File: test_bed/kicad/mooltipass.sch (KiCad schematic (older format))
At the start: 14 parts, among them CON1 AVR-ISP-6, P1 CONN_8, P2 CONN_6, P3 CONN_10, P4 CONN_8, P5 CONN_1, P6 CONN_1, P7 CONN_1, P8 CONN_1

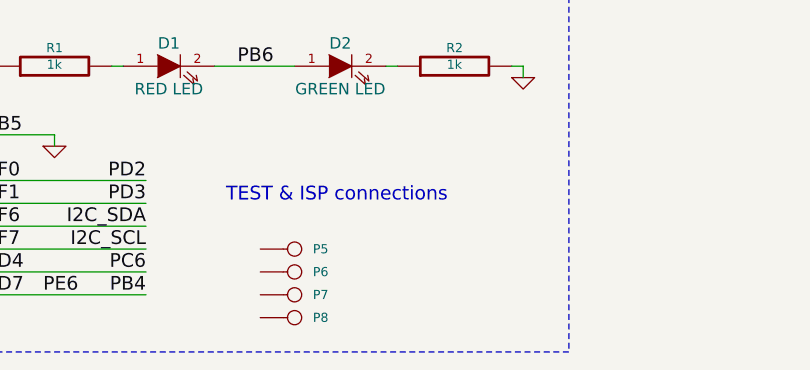
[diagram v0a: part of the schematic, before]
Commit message: mooltipass electrical test bed complete
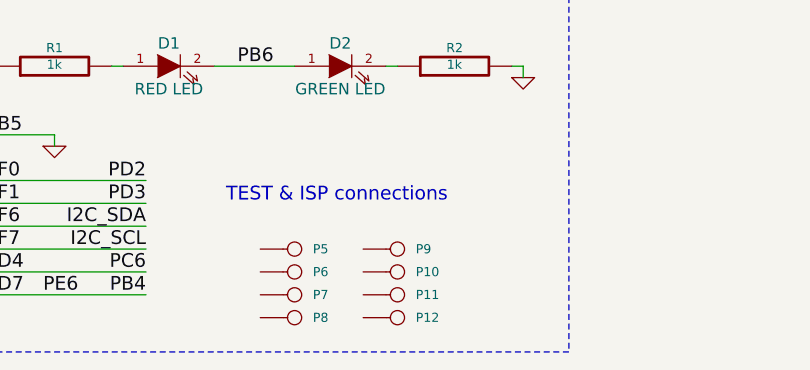
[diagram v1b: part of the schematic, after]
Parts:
- added P10, P11, P12, P9: CONN_1, symbol CONN_1
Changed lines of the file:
@@
 A5
 $Comp
-L +5V #PWR01
+L +5V #PWR3
 U 1 1 53011242
 P 2150 3600
-F 0 "#PWR01" H 2150 3690 20  0001 C CNN
+F 0 "#PWR3" H 2150 3690 20  0001 C CNN
 F 1 "+5V" H 2150 3690 30  0000 C CNN
 F 2 "" H 2150 3600 60  0000 C CNN
@@
 $EndComp
 $Comp
-L GND #PWR02
+L GND #PWR2
 U 1 1 5301124C
 P 2000 4400
-F 0 "#PWR02" H 2000 4400 30  0001 C CNN
+F 0 "#PWR2" H 2000 4400 30  0001 C CNN
 F 1 "GND" H 2000 4330 30  0001 C CNN
 F 2 "" H 2000 4400 60  0000 C CNN
@@
 NoConn ~ 1950 3650
 $Comp
-L +3.3V #PWR03
+L +3.3V #PWR1
 U 1 1 530118E2
 P 2000 3600
-F 0 "#PWR03" H 2000 3560 30  0001 C CNN
+F 0 "#PWR1" H 2000 3560 30  0001 C CNN
 F 1 "+3.3V" H 2000 3710 30  0000 C CNN
 F 2 "" H 2000 3600 60  0000 C CNN
@@
 AREF
 $Comp
-L GND #PWR04
+L GND #PWR4
 U 1 1 53011EED
 P 3050 4200
-F 0 "#PWR04" H 3050 4200 30  0001 C CNN
+F 0 "#PWR4" H 3050 4200 30  0001 C CNN
 F 1 "GND" H 3050 4130 30  0001 C CNN
 F 2 "" H 3050 4200 60  0000 C CNN
@@
 	5500 3250 5500 3175
 $Comp
-L +5V #PWR05
+L +5V #PWR7
 U 1 1 54F1E42B
 P 5500 3175
-F 0 "#PWR05" H 5500 3265 20  0001 C CNN
+F 0 "#PWR7" H 5500 3265 20  0001 C CNN
 F 1 "+5V" H 5500 3265 30  0000 C CNN
 F 2 "" H 5500 3175 60  0000 C CNN
@@
 $EndComp
 $Comp
-L GND #PWR06
+L GND #PWR8
 U 1 1 54F1E431
 P 5500 3525
-F 0 "#PWR06" H 5500 3525 30  0001 C CNN
+F 0 "#PWR8" H 5500 3525 30  0001 C CNN
 F 1 "GND" H 5500 3455 30  0001 C CNN
 F 2 "" H 5500 3525 60  0000 C CNN
@@
 $EndComp
 $Comp
-L +5V #PWR07
+L +5V #PWR5
 U 1 1 54F1EB3C
 P 4400 3900
-F 0 "#PWR07" H 4400 3990 20  0001 C CNN
+F 0 "#PWR5" H 4400 3990 20  0001 C CNN
 F 1 "+5V" H 4400 3990 30  0000 C CNN
 F 2 "" H 4400 3900 60  0000 C CNN
@@
 $EndComp
 $Comp
-L GND #PWR08
+L GND #PWR11
 U 1 1 54F1EB4F
 P 6750 4000
-F 0 "#PWR08" H 6750 4000 30  0001 C CNN
+F 0 "#PWR11" H 6750 4000 30  0001 C CNN
 F 1 "GND" H 6750 3930 30  0001 C CNN
 F 2 "" H 6750 4000 60  0000 C CNN
@@
 PF7
 $Comp
-L GND #PWR09
+L GND #PWR6
 U 1 1 54F1EEA6
 P 4700 4300
-F 0 "#PWR09" H 4700 4300 30  0001 C CNN
+F 0 "#PWR6" H 4700 4300 30  0001 C CNN
 F 1 "GND" H 4700 4230 30  0001 C CNN
 F 2 "" H 4700 4300 60  0000 C CNN
@@
 $EndComp
 $Comp
-L +5V #PWR010
+L +5V #PWR9
 U 1 1 54F1F4C3
 P 6500 3150
-F 0 "#PWR010" H 6500 3240 20  0001 C CNN
+F 0 "#PWR9" H 6500 3240 20  0001 C CNN
 F 1 "+5V" H 6500 3240 30  0000 C CNN
 F 2 "" H 6500 3150 60  0000 C CNN
@@
 $EndComp
 $Comp
-L GND #PWR011
+L GND #PWR10
 U 1 1 54F1F4C9
 P 6500 3550
-F 0 "#PWR011" H 6500 3550 30  0001 C CNN
+F 0 "#PWR10" H 6500 3550 30  0001 C CNN
 F 1 "GND" H 6500 3480 30  0001 C CNN
 F 2 "" H 6500 3550 60  0000 C CNN
@@
 	1    0    0    -1
 $EndComp
+$Comp
+L CONN_1 P9
+U 1 1 54F21912
+P 6200 4750
+F 0 "P9" H 6280 4750 40  0000 L CNN
+F 1 "CONN_1" H 6200 4805 30  0001 C CNN
+F 2 "" H 6200 4750 60  0000 C CNN
+F 3 "" H 6200 4750 60  0000 C CNN
+	1    6200 4750
+	1    0    0    -1
+$EndComp
+$Comp
+L CONN_1 P10
+U 1 1 54F21918
+P 6200 4850
+F 0 "P10" H 6280 4850 40  0000 L CNN
+F 1 "CONN_1" H 6200 4905 30  0001 C CNN
+F 2 "" H 6200 4850 60  0000 C CNN
+F 3 "" H 6200 4850 60  0000 C CNN
+	1    6200 4850
+	1    0    0    -1
+$EndComp
+$Comp
+L CONN_1 P11
+U 1 1 54F2191E
+P 6200 4950
+F 0 "P11" H 6280 4950 40  0000 L CNN
+F 1 "CONN_1" H 6200 5005 30  0001 C CNN
+F 2 "" H 6200 4950 60  0000 C CNN
+F 3 "" H 6200 4950 60  0000 C CNN
+	1    6200 4950
+	1    0    0    -1
+$EndComp
+$Comp
+L CONN_1 P12
+U 1 1 54F21924
+P 6200 5050
+F 0 "P12" H 6280 5050 40  0000 L CNN
+F 1 "CONN_1" H 6200 5105 30  0001 C CNN
+F 2 "" H 6200 5050 60  0000 C CNN
+F 3 "" H 6200 5050 60  0000 C CNN
+	1    6200 5050
+	1    0    0    -1
+$EndComp
